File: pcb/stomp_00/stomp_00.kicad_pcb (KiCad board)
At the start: 2 copper layers, 54 x 106 mm, 41 parts, among them J1 9V_Power_Input, J10 AudioJack3, J11 AudioJack3, J2 GuitarInput1, J3 GuitarOutput1, J4 Headphones, J7 GuitarInput2, J8 Conn_01x09_Pin, SW1 SW_DIP_x04, SW2 SW_3PDT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

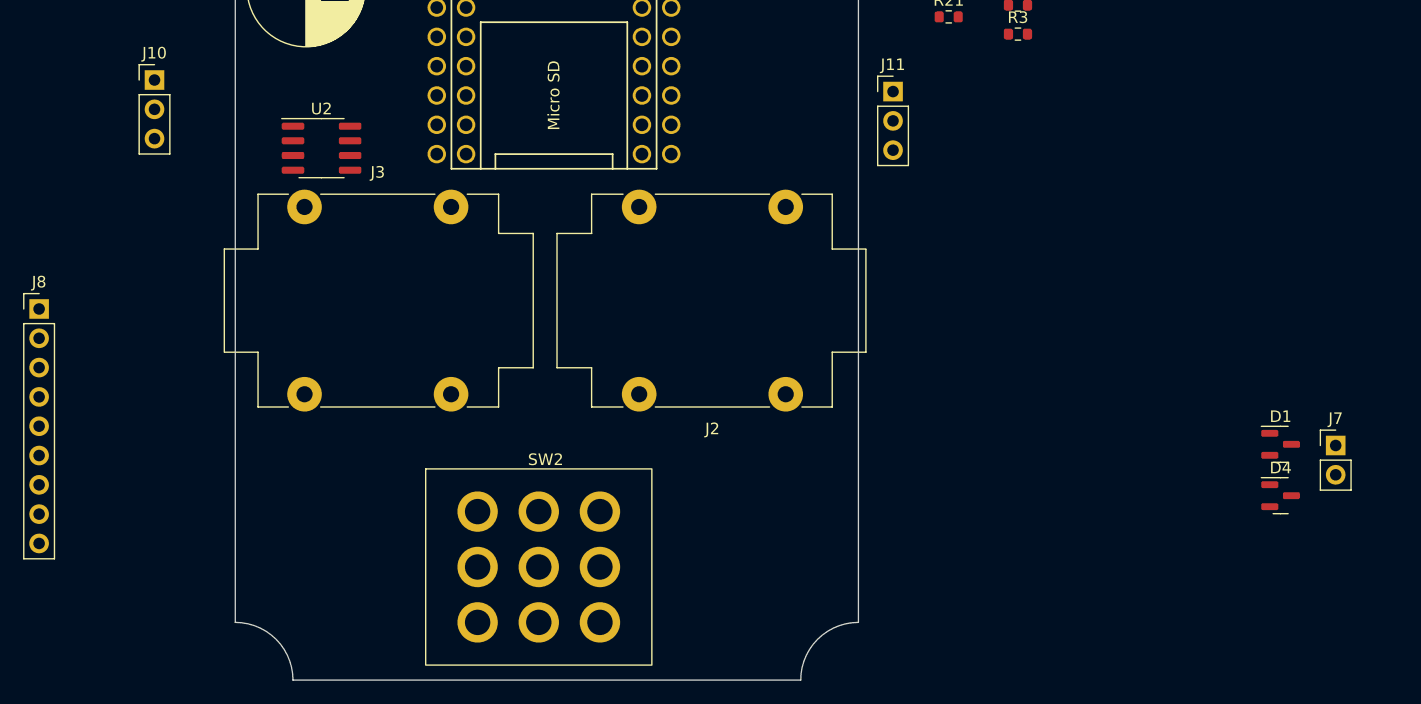
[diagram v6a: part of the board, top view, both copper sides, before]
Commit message: footswitch routing
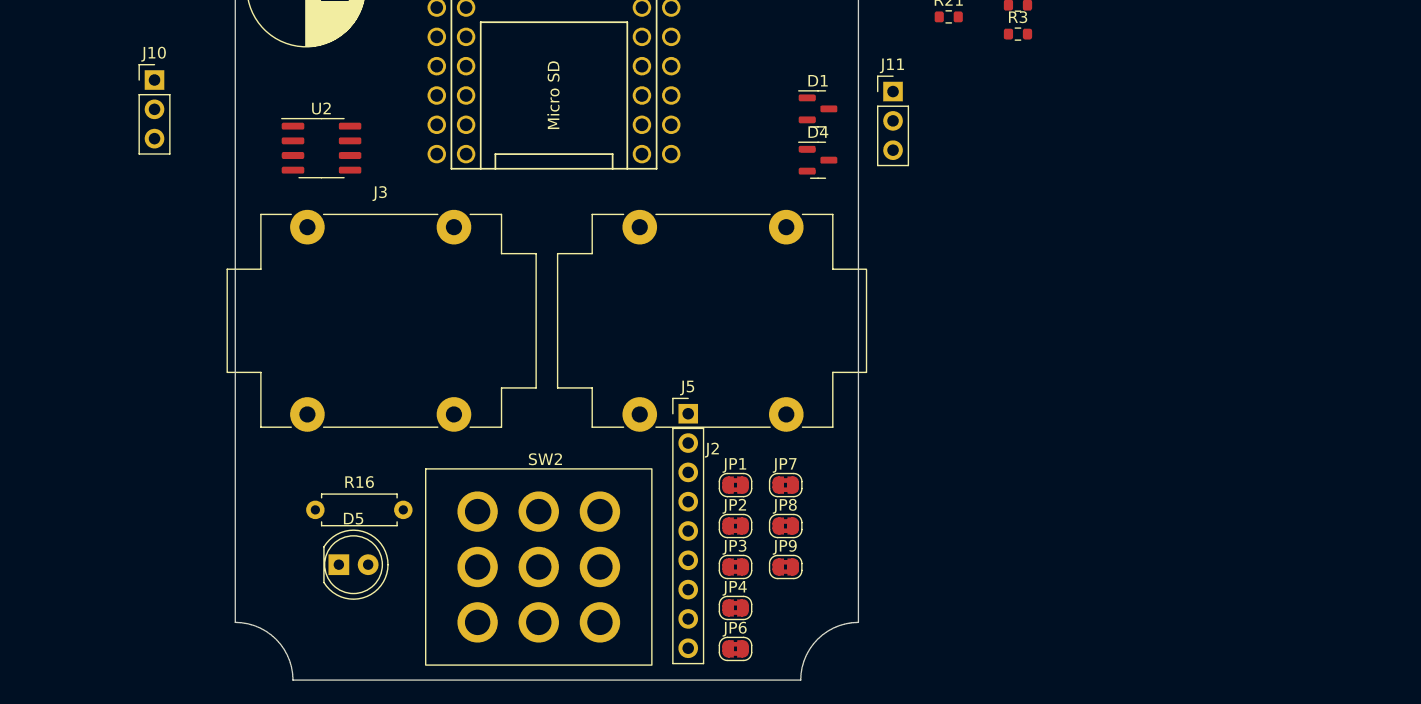
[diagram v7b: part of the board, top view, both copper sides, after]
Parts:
- removed J7: GuitarInput2, Connector_PinHeader_2.54mm:PinHeader_1x02_P2.54mm_Vertical
- removed J8: Conn_01x09_Pin, Connector_PinHeader_2.54mm:PinHeader_1x09_P2.54mm_Vertical
- added D5: LED, LED_THT:LED_D5.0mm, F.Cu at (8.97, 96.0)
- added J5: Conn_01x09_Pin, Connector_PinHeader_2.54mm:PinHeader_1x09_P2.54mm_Vertical, F.Cu at (39.2, 82.9)
- added JP1: Jumper_2_Bridged, Jumper:SolderJumper-2_P1.3mm_Bridged2Bar_RoundedPad1.0x1.5mm, F.Cu at (43.4, 89.1)
- added JP2: Jumper_2_Bridged, Jumper:SolderJumper-2_P1.3mm_Bridged2Bar_RoundedPad1.0x1.5mm, F.Cu at (43.4, 92.7)
- added JP3: Jumper_2_Bridged, Jumper:SolderJumper-2_P1.3mm_Bridged2Bar_RoundedPad1.0x1.5mm, F.Cu at (43.4, 96.2)
- added JP4: Jumper_2_Bridged, Jumper:SolderJumper-2_P1.3mm_Bridged2Bar_RoundedPad1.0x1.5mm, F.Cu at (43.4, 99.8)
- added JP6: Jumper_2_Bridged, Jumper:SolderJumper-2_P1.3mm_Bridged2Bar_RoundedPad1.0x1.5mm, F.Cu at (43.4, 103.3)
- added JP7: Jumper_2_Bridged, Jumper:SolderJumper-2_P1.3mm_Bridged2Bar_RoundedPad1.0x1.5mm, F.Cu at (47.7, 89.1)
- added JP8: Jumper_2_Bridged, Jumper:SolderJumper-2_P1.3mm_Bridged2Bar_RoundedPad1.0x1.5mm, F.Cu at (47.7, 92.7)
- added JP9: Jumper_2_Bridged, Jumper:SolderJumper-2_P1.3mm_Bridged2Bar_RoundedPad1.0x1.5mm, F.Cu at (47.7, 96.2)
- added R16: R_US, Resistor_THT:R_Axial_DIN0207_L6.3mm_D2.5mm_P7.62mm_Horizontal, F.Cu at (6.94, 91.2)
- SW2: value SW_3PDT -> Footswitch
- moved D1 49.5 mm to (50.5, 56.5)
- moved D4 49.5 mm to (50.5, 61.0)
- moved J3 1.77 mm to (6.25, 66.8)
- moved J2 1.75 mm to (47.8, 83.0)
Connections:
- J3 pad S: unconnected-(J3-PadS) -> GNDA
- J3 pad SN: unconnected-(J3-PadSN) -> GNDA
- J3 pad T: unconnected-(J3-PadT) -> Net-(JP8-A)
- J3 pad TN: unconnected-(J3-PadTN) -> GNDA
- SW2 pad 1: Net-(J8-Pin_1) -> FOOTSWITCH_1
- SW2 pad 2: Net-(J8-Pin_2) -> FOOTSWITCH_2
- SW2 pad 3: Net-(J8-Pin_3) -> FOOTSWITCH_3
- SW2 pad 4: Net-(J8-Pin_4) -> FOOTSWITCH_4
- SW2 pad 5: Net-(J8-Pin_5) -> FOOTSWITCH_5
- SW2 pad 6: Net-(J8-Pin_6) -> FOOTSWITCH_6
- SW2 pad 7: Net-(J8-Pin_7) -> FOOTSWITCH_7
- SW2 pad 8: Net-(J8-Pin_8) -> FOOTSWITCH_8
- SW2 pad 9: Net-(J8-Pin_9) -> FOOTSWITCH_9

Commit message: pcb...
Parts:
- removed H3, H4: MountingHole, MountingHole:MountingHole_3.2mm_M3
- removed RV4, RV5, RV6: R_Potentiometer_US, Potentiometer_THT:Potentiometer_Piher_PC-16_Single_Vertical
- added J6: Conn_01x09, Connector_PinHeader_2.54mm:PinHeader_1x09_P2.54mm_Vertical, F.Cu at (31.5, 85.8)
- added J7: Conn_02x04_Counter_Clockwise, Connector_PinHeader_2.54mm:PinHeader_2x04_P2.54mm_Vertical, F.Cu at (46.5, 8.13)
- added JP5: Jumper_2_Bridged, Jumper:SolderJumper-2_P1.3mm_Bridged2Bar_RoundedPad1.0x1.5mm, F.Cu at (60.3, 121.3)
- J2: value GuitarInput1 -> Conn_01x09; footprint Connector_Audio:Jack_6.35mm_Neutrik_NMJ4HCD2_Horizontal -> Connector_PinHeader_2.54mm:PinHeader_1x09_P2.54mm_Vertical
- J3: value GuitarOutput1 -> GuitarInput1
- J5: value Conn_01x09_Pin -> GuitarOutput1; footprint Connector_PinHeader_2.54mm:PinHeader_1x09_P2.54mm_Vertical -> Connector_Audio:Jack_6.35mm_Neutrik_NMJ4HCD2_Horizontal
- JP9: value Jumper_2_Bridged -> Jumper_2_Open; footprint Jumper:SolderJumper-2_P1.3mm_Bridged2Bar_RoundedPad1.0x1.5mm -> Jumper:SolderJumper-2_P1.3mm_Open_RoundedPad1.0x1.5mm
- SW1: moved to B.Cu
- moved H2 139.2 mm to (50.0, 98.0)
- moved J10 103.2 mm to (96.0, 60.0)
- moved H1 89.0 mm to (4.00, 8.00)
- moved U14 64.5 mm to (100.0, 50.7)
- moved R16 61.2 mm to (55.4, 128.6)
- moved J11 47.0 mm to (103.8, 60.2)
- moved J2 45.4 mm to (2.46, 85.8), turned to 90 degrees
- moved D3 44.1 mm to (108.8, 55.0)
- moved J3 43.9 mm to (47.7, 81.4), turned to 180 degrees
- moved J5 37.4 mm to (6.32, 65.1)
- moved JP7 33.3 mm to (64.7, 117.7)
- moved JP8 33.3 mm to (64.7, 121.3)
- moved JP9 33.3 mm to (64.7, 124.8)
- moved JP1 31.3 mm to (56.0, 117.7)
- moved JP2 31.3 mm to (56.0, 121.3)
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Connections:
- J3 pad T: Net-(JP8-A) -> Net-(J6-Pin_1)
- JP2 pad 1: FOOTSWITCH_5 -> FOOTSWITCH_2
- JP2 pad 2: GNDA -> Net-(J6-Pin_1)
- JP3 pad 1: FOOTSWITCH_2 -> FOOTSWITCH_3
- JP3 pad 2: Net-(JP3-B) -> INSTRUMENT_IN_L
- JP4 pad 1: FOOTSWITCH_3 -> FOOTSWITCH_5
- JP4 pad 2: INSTRUMENT_IN_L -> GNDA
- JP6 pad 1: FOOTSWITCH_6 -> Net-(JP1-B)
- JP6 pad 2: Net-(D5-K) -> FOOTSWITCH_7
- JP7 pad 1: Net-(JP1-B) -> Net-(JP7-A)
- JP7 pad 2: FOOTSWITCH_7 -> FOOTSWITCH_8
- JP8 pad 1: Net-(JP8-A) -> LINE_OUT_L
- JP8 pad 2: FOOTSWITCH_8 -> FOOTSWITCH_9
- JP9 pad 1: LINE_OUT_L -> INSTRUMENT_IN_L
- JP9 pad 2: FOOTSWITCH_9 -> Net-(J6-Pin_1)
